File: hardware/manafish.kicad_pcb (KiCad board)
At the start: 2 copper layers, 70 x 100 mm, 75 parts, among them IC1 BMI270, IC2 SHT45-AD1F-R2, J1 Conn_01x04_Pin, J2 SM03B-SRSS-TB, J3 AM32_1, J4 AM32_2, J5 Conn_01x22_Female, J6 Battery, J7 Conn_02x07_Odd_Even, J8 USB_C_Receptacle_USB2.0_14P, U1 TPD4EUSB30, U2 TPD4EUSB30, U3 MagJack-A70-112-331N126, U4 RP2354A, U5 Ag59824-LPB, U6 PC817, U7 PC817, Y1 ABM8-272-T3

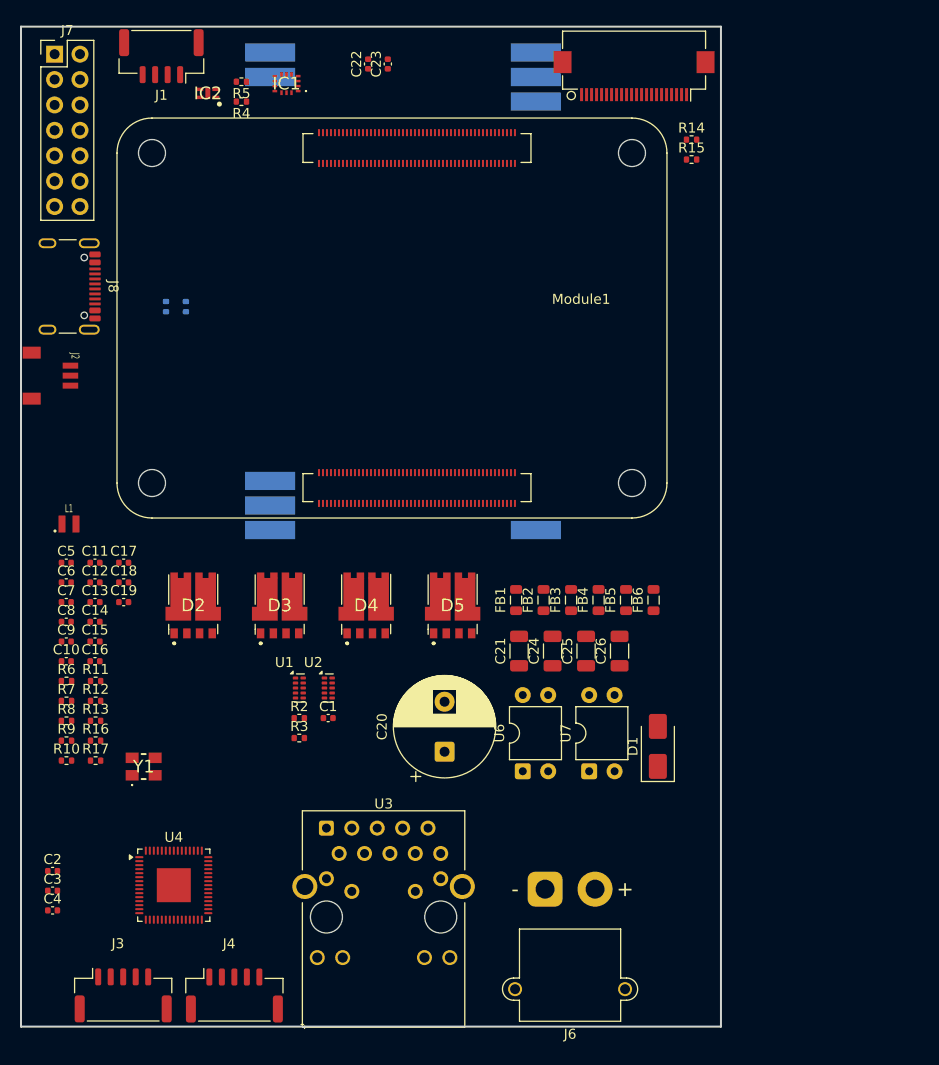
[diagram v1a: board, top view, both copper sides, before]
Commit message: Lay out the 4-layer PCB
Route the board on JLCPCB's JLC04161H-7628 stackup (4 layers, 1.6 mm,
ENIG). It fits a 74 mm tube centred on its axis; the tightest part is the
USB-C port J8, 1.8 mm from the wall. DRC gives 0 errors, 0 unconnected
items and a clean schematic parity check. 21 advisory warnings remain on
the 3 mm PoE isolation guide; the README lists them.

Layout:
- the PoE primary side keeps 2.0 mm from everything else on every layer,
  enforced by manafish.kicad_dru, with a primary-only island under U5's
  input half and inner-layer voids next to primary copper
- 100 ohm (Ethernet, CSI) and 90 ohm (USB) pair classes over a solid In1
  ground; GND pours on all layers with stitching vias
- RP2354A core regulator laid out per the RP2350 datasheet, including the
  In1 cut-out under VREG_LX
- fabrication, assembly and isolation-test notes on User.Comments

Schematic and BOM:
- U3 is now the YAGEO JXF0-1012NL 4-pair PoE MagJack, with a new YAGEO
  library and STEP model drawn from datasheet J520
- C21/C24 are 4.7 nF 2 kV KEMET C1812X472KGRACTU (1812)
- U6/U7 are LTV-817S-TA1 (SMD)
- J8's four VBUS pins are joined by a local VBUS label

Libraries:
- Silvertel Ag59800: keep-out on the module-facing layer and the inner
  layer next to it; pads 1-3, 8 and 9 solder-mask defined
- LTC4162 QFN: the exposed-pad paste windows clear the thermal vias
- ABM8-272-T3 courtyard trimmed; 3D model paths fixed for ABM8, SHT45 and
  BMI270

README: new PCB section (stackup, impedance, isolation, assembly,
testing) and the power and Ethernet descriptions brought up to date.
NOTICE: the YAGEO files and the library changes.

Co-Authored-By: Claude Opus 5.5 <noreply@anthropic.com>
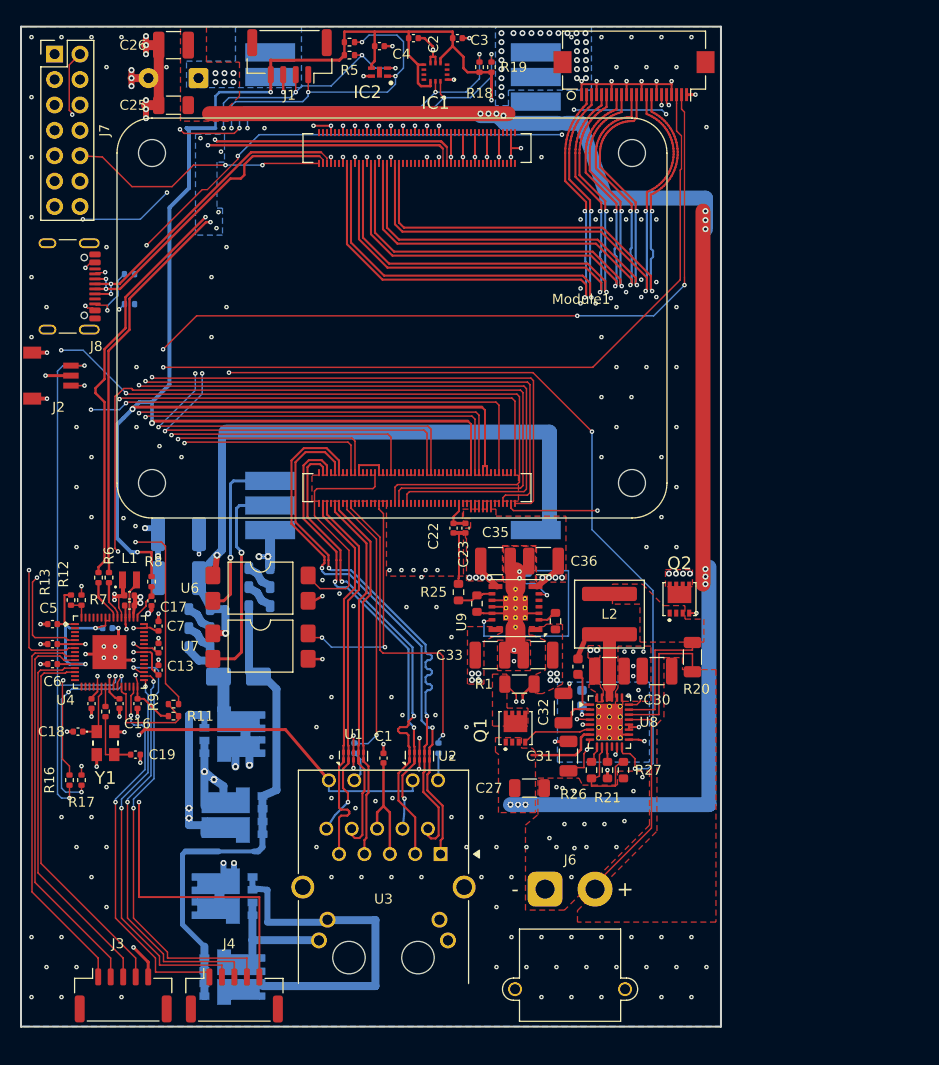
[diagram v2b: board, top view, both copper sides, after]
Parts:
- added C27: 100nF 50V, Capacitor_SMD:C_1206_3216Metric, F.Cu at (138.0, 124.6)
- added C28: 10uF 50V, Capacitor_SMD:C_1210_3225Metric, F.Cu at (146.0, 112.9)
- added C29: 22nF 50V, Capacitor_SMD:C_0603_1608Metric, F.Cu at (142.8, 112.5)
- added C30: 10uF 50V, Capacitor_SMD:C_1210_3225Metric, F.Cu at (150.8, 112.9)
- added C31: 1uF 50V, Capacitor_SMD:C_1206_3216Metric, F.Cu at (141.9, 121.4)
- added C32: 4.7uF 50V, Capacitor_SMD:C_1206_3216Metric, F.Cu at (141.4, 116.6)
- added C33: 10uF 50V, Capacitor_SMD:C_1210_3225Metric, F.Cu at (134.1, 111.3)
- added C34: 10uF 50V, Capacitor_SMD:C_1210_3225Metric, F.Cu at (138.8, 111.3)
- added C35: 47uF 10V, Capacitor_SMD:C_1210_3225Metric, F.Cu at (134.6, 101.9)
- added C36: 47uF 10V, Capacitor_SMD:C_1210_3225Metric, F.Cu at (139.4, 101.9)
- added C37: 100nF 50V, Capacitor_SMD:C_0603_1608Metric, B.Cu at (143.2, 115.6)
- added L2: 6.8uH, Inductor_SMD:L_Coilcraft_XAL6060-XXX, F.Cu at (146.0, 107.2)
- added Q1: FDMC8327L, FDMC86139P:FDMC86139P, F.Cu at (136.6, 118.6)
- added Q2: FDMC8327L, FDMC86139P:FDMC86139P, F.Cu at (153.0, 105.7)
- added R1: 16mR, Resistor_SMD:R_1206_3216Metric, F.Cu at (137.0, 114.2)
- added R20: 10mR, Resistor_SMD:R_1206_3216Metric, F.Cu at (154.3, 111.5)
- added R21: 63.4kR, Resistor_SMD:R_0603_1608Metric, F.Cu at (145.8, 122.8)
- added R22: 100kR, Resistor_SMD:R_0603_1608Metric, F.Cu at (140.6, 107.9)
- added R23: 100kR, Resistor_SMD:R_0603_1608Metric, B.Cu at (137.0, 103.0)
- added R24: 2.49kR, Resistor_SMD:R_0603_1608Metric, F.Cu at (132.8, 106.2)
- added R25: 10kR, Resistor_SMD:R_0603_1608Metric, F.Cu at (130.9, 105.0)
- added R26: 10kR, Resistor_SMD:R_0603_1608Metric, F.Cu at (144.2, 122.8)
- added R27: 10kR, Resistor_SMD:R_0603_1608Metric, F.Cu at (147.4, 122.8)
- added U8: LTC4162-LAD, LTC4162:QFN-28-1EP_4x5mm_P0.5mm_EP2.65x3.65mm_ThermalVias0.3mm, F.Cu at (146.0, 118.0)
- added U9: TPSM53603RDA, Package_DFN_QFN:Texas_B3QFN-14-1EP_5x5.5mm_P0.65mm_ThermalVia, F.Cu at (136.6, 106.6)
- C11, D1, D2, D3, D4, D5, FB1, FB2, FB3, FB4, FB5, FB6, R14, R15, R2, R3: moved to B.Cu
- C20: value 470uF 25V -> 470uF 35V; moved to B.Cu
- C21, C24: footprint Capacitor_SMD:C_1206_3216Metric -> Capacitor_SMD:C_1812_4532Metric; moved to B.Cu
- C25: value 100nF 25V -> 100nF 50V
- C26: value 10uF 25V -> 10uF 50V; footprint Capacitor_SMD:C_1206_3216Metric -> Capacitor_SMD:C_1210_3225Metric
- R18, R19: moved to F.Cu
- U3: value MagJack-A70-112-331N126 -> JXF0-1012NL; footprint CM5IO:TRJG0926HENL -> YAGEO:YAGEO_JXF0-1012NL
- U6, U7: value PC817 -> LTV-817S; footprint Package_DIP:DIP-4_W7.62mm -> Package_DIP:SMDIP-4_W9.53mm_Clearance8mm
- moved C3 94.4 mm to (130.8, 49.6)
- moved C4 92.4 mm to (123.0, 50.4)
- moved C2 90.8 mm to (126.4, 49.6)
- moved C26 75.2 mm to (102.4, 50.3), turned to 180 degrees
- moved C20 71.7 mm to (104.9, 53.6), turned to 180 degrees
- moved C25 68.4 mm to (102.4, 56.3), turned to 180 degrees
- moved R15 58.0 mm to (98.0, 76.2)
- moved R14 57.8 mm to (98.0, 73.2)
- moved C22 47.2 mm to (130.4, 98.6)
- moved C23 47.1 mm to (131.6, 98.6)
- moved FB6 45.4 mm to (105.0, 106.7), turned to 0 degrees
- moved D5 43.2 mm to (108.4, 143.5), turned to 90 degrees
- moved FB5 42.8 mm to (105.0, 108.6), turned to 0 degrees
- moved D1 42.5 mm to (108.9, 113.5), turned to 0 degrees
- moved FB4 40.2 mm to (105.0, 110.5), turned to 0 degrees
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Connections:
- J6 pad 1: /Power Management/BAT- -> GND
- J8 pad A4: unconnected-(J8-VBUS-PadA4)_3 -> /VBUS
- J8 pad A9: unconnected-(J8-VBUS-PadA4)_1 -> /VBUS
- J8 pad B4: unconnected-(J8-VBUS-PadA4)_2 -> /VBUS
- J8 pad B9: unconnected-(J8-VBUS-PadA4) -> /VBUS
- U3 pad 11: /Ethernet/VC1 -> /RP2354A/VREG_VIN
- U3 pad 12: /Ethernet/VC2 -> Net-(U3-LEDG_K)
- U3 pad 13: /Ethernet/VC3 -> /RP2354A/VREG_VIN
- U3 pad 14: /Ethernet/VC4 -> Net-(U3-LEDY_K)
- U3 pad 15: /RP2354A/VREG_VIN -> /Ethernet/VC1
- U3 pad 16: Net-(U3-LEDY_K) -> /Ethernet/VC4
- U3 pad 17: /RP2354A/VREG_VIN -> /Ethernet/VC2
- U3 pad 18: Net-(U3-LEDG_K) -> /Ethernet/VC3
- U3 pad 4: Net-(C1-Pad1) -> /Ethernet/TRD1_N
- U3 pad 6: /Ethernet/TRD1_N -> Net-(C1-Pad1)
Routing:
- net /RP2354A/VREG_VIN: track 0.00 -> 316.9 mm, vias 0 -> 16
- net /I2C Peripherals/I2C1_SCL: track 0.00 -> 199.9 mm, vias 0 -> 9
- net /I2C Peripherals/I2C1_SDA: track 0.00 -> 183.1 mm, vias 0 -> 9
- net GND: track 0.00 -> 164.4 mm, vias 0 -> 286
- net /Power Management/24V: track 0.00 -> 149.4 mm, vias 0 -> 19
- net /Camera Serial Interface/CAM_GPIO1: track 0.00 -> 125.1 mm, vias 0 -> 5
- net /Camera Serial Interface/SDA0: track 0.00 -> 121.5 mm, vias 0 -> 4
- net /Camera Serial Interface/SCL0: track 0.00 -> 118.3 mm, vias 0 -> 2
- net /I2C Peripherals/I2C0_SDA: track 0.00 -> 117.1 mm, vias 0 -> 4
- net /RP2354A/RP2354_SWDIO: track 0.00 -> 117.0 mm, vias 0 -> 3
- net /I2C Peripherals/I2C0_SCL: track 0.00 -> 102.3 mm, vias 0 -> 7
- net /RP2354A/RUN: track 0.00 -> 100.2 mm, vias 0 -> 2
- net /Rasperry Pi Compute Module 5/nRPIBOOT: track 0.00 -> 90.0 mm, vias 0 -> 2
- net /RP2354A/BOOTSEL: track 0.00 -> 86.2 mm, vias 0 -> 2
- net /Rasperry Pi Compute Module 5/PMIC_ENABLE: track 0.00 -> 74.9 mm, vias 0 -> 1
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- added copper zone on F.Cu, net /Power Management/+5V
- added copper zone on In2.Cu, net /Power Management/+5V
- added copper zone on B.Cu, net /Power Management/24V
- added copper zone on F.Cu, net /Power Management/24V
- added copper zone on F.Cu, net /Power Management/BAT+
- added copper zone on F.Cu, net /Power Management/VSYS
- added copper zone on In2.Cu, net /Power Management/VSYS
- added copper zone on In2.Cu, net /RP2354A/VREG_VIN
- added copper zone on B.Cu, net GND
- added copper zone on F.Cu, net GND
- added copper zone on In1.Cu, net GND
- added copper zone on In2.Cu, net GND
- added copper zone on F.Cu, net Net-(Q1-D_1)
- added copper zone on F.Cu, net Net-(Q2-S_1)
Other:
- copper layers 2 -> 4
- board text added: "FABRICATION JLCPCB 4 layers, 1.6 mm, stackup JLC04161H-7628, 1 oz outer / 0.5 oz inner, ENIG. Vias tented; the exposed-pad vias of U4, U8 and U9 stay open (their paste windows keep clear of the holes). Impedance control +-10 %: L1/L4 100 ohm differential, 0.21 mm / 0.19 mm gap (Ethernet TRD*, CSI DPHY0_*); L1 90 ohm differential, 0.24 mm / 0.15 mm gap (USB). Min track 0.1 mm, min via 0.45/0.2 mm.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"

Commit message: Add second camera, magnet load switch and schematic fixes
- Second camera J11 on MIPI1: I2C on ID_SD/ID_SC with 2.2k pull-ups,
  power enable on GPIO14/15 (CAM1_GPIO0/1); both cameras take 3.3 V
  from CM5_3.3V
- Magnet power switch: IC9 output is now +5V_AON, TPS22965 load switch
  IC15 drives +5V, J12 carries +5V_AON / MAG_ON / GND with R29
  pull-down; new TPS22965 symbol library
- Power: 4 A TPSM53604, 8 mOhm input sense resistor, C39/C40 bulk caps,
  F1-F3 battery polyfuses; 5 V raised to 5.115 V (R24 2.43k, 0.5 %
  feedback resistors); 47 uF at the CM5 5 V pins
- BMI270 on SPI and WSEN-PADS on I2C in serial_peripherals.kicad_sch
- Breakout headers J9/J13 with 5 V, 3.3 V and GND
- References renamed U -> IC; net classes for DPHY1, +5V, +5V_AON, +3.3V
- ERC clean (0 errors, 0 warnings); PCB update from the schematic is
  still in progress

Co-Authored-By: Claude Opus 5.5 <noreply@anthropic.com>
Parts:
- added C38: 100n, Capacitor_SMD:C_0402_1005Metric, F.Cu at (174.4, 140.1)
- added IC10: WSEN-PADS_2511020213301, Package_LGA:ST_HLGA-10_2x2mm_P0.5mm_LayoutBorder3x2y, F.Cu at (174.8, 137.4)
- added J9: Conn_02x08_Odd_Even, Connector_PinHeader_1.27mm:PinHeader_2x08_P1.27mm_Vertical, F.Cu at (167.6, 137.2)
- J7: footprint Connector_PinHeader_2.54mm:PinHeader_2x07_P2.54mm_Vertical -> Connector_PinHeader_1.27mm:PinHeader_2x07_P1.27mm_Vertical
- renumbered U1 to IC1, IC1 to IC11, IC2 to IC12, U2 to IC2, U3 to IC3, U4 to IC4, U5 to IC5, U6 to IC6, U7 to IC7, U8 to IC8, U9 to IC9
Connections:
- Module1 pad 24: unconnected-(Module1A-GPIO26-Pad24) -> /I2C Peripherals/INT_DRDY
- Module1 pad 25: unconnected-(Module1A-GPIO21-Pad25) -> /Rasperry Pi Compute Module 5/GPIO21
- Module1 pad 26: unconnected-(Module1A-GPIO19-Pad26) -> /Rasperry Pi Compute Module 5/GPIO19
- Module1 pad 27: unconnected-(Module1A-GPIO20-Pad27) -> /Rasperry Pi Compute Module 5/GPIO20
- Module1 pad 28: unconnected-(Module1A-GPIO13-Pad28) -> /Rasperry Pi Compute Module 5/GPIO13
- Module1 pad 29: unconnected-(Module1A-GPIO16-Pad29) -> /Rasperry Pi Compute Module 5/GPIO16
- Module1 pad 34: unconnected-(Module1A-GPIO5-Pad34) -> /Rasperry Pi Compute Module 5/GPIO5
- Module1 pad 37: unconnected-(Module1A-GPIO7-Pad37) -> /Rasperry Pi Compute Module 5/GPIO7
- Module1 pad 40: unconnected-(Module1A-GPIO9-Pad40) -> /Rasperry Pi Compute Module 5/GPIO9
- Module1 pad 44: unconnected-(Module1A-GPIO10-Pad44) -> /Rasperry Pi Compute Module 5/GPIO10
- Module1 pad 46: unconnected-(Module1A-GPIO22-Pad46) -> /Rasperry Pi Compute Module 5/GPIO22
- Module1 pad 47: unconnected-(Module1A-GPIO23-Pad47) -> /Rasperry Pi Compute Module 5/GPIO23
- Module1 pad 48: unconnected-(Module1A-GPIO27-Pad48) -> /Rasperry Pi Compute Module 5/GPIO27
- Module1 pad 49: unconnected-(Module1A-GPIO18-Pad49) -> /Rasperry Pi Compute Module 5/GPIO18
- Module1 pad 50: unconnected-(Module1A-GPIO17-Pad50) -> /Rasperry Pi Compute Module 5/GPIO17
- Module1 pad 51: unconnected-(Module1A-GPIO15-Pad51) -> /Rasperry Pi Compute Module 5/GPIO15
- Module1 pad 54: unconnected-(Module1A-GPIO4-Pad54) -> /Rasperry Pi Compute Module 5/GPIO4
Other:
- board text added: "FABRICATION JLCPCB 4 layers, 1.6 mm, stackup JLC04161H-7628, 1 oz outer / 0.5 oz inner, ENIG. Vias tented; the exposed-pad vias of IC4, IC8 and IC9 stay open (their paste windows keep clear of the holes). Impedance control +-10 %: L1/L4 100 ohm differential, 0.21 mm / 0.19 mm gap (Ethernet TRD*, CSI DPHY0_*); L1 90 ohm differential, 0.24 mm / 0.15 mm gap (USB). Min track 0.1 mm, min via 0.45/0.2 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"
- board text removed: "FABRICATION JLCPCB 4 layers, 1.6 mm, stackup JLC04161H-7628, 1 oz outer / 0.5 oz inner, ENIG. Vias tented; the exposed-pad vias of U4, U8 and U9 stay open (their paste windows keep clear of the holes). Impedance control +-10 %: L1/L4 100 ohm differential, 0.21 mm / 0.19 mm gap (Ethernet TRD*, CSI DPHY0_*); L1 90 ohm differential, 0.24 mm / 0.15 mm gap (USB). Min track 0.1 mm, min via 0.45/0.2 mm.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"
